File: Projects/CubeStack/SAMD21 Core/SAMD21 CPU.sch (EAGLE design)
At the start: 38 parts, among them Q1 MBT3904DW2T1, Q2 SI2347DS, Q3 SI2347DS, U1 ATSAMD21G-A, U2 SST26VF064B, U3 AZ1117C, X1A PINHD-1X10, X1B PINHD-1X10, X1C PINHD-1X10, X1D PINHD-1X10, X2 10PIN_CORTEX_DEBUGTHRU_HOLE, Y1 FC1610AN

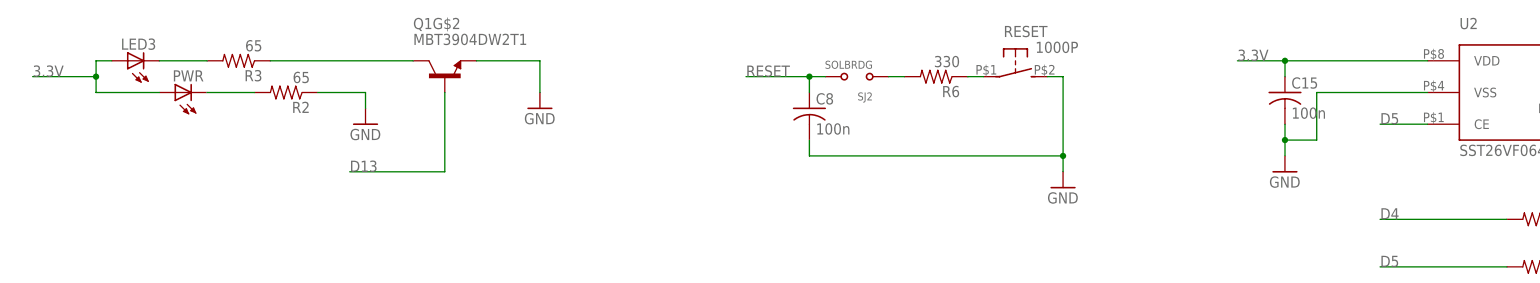
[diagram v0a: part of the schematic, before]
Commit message: Changed C9 package
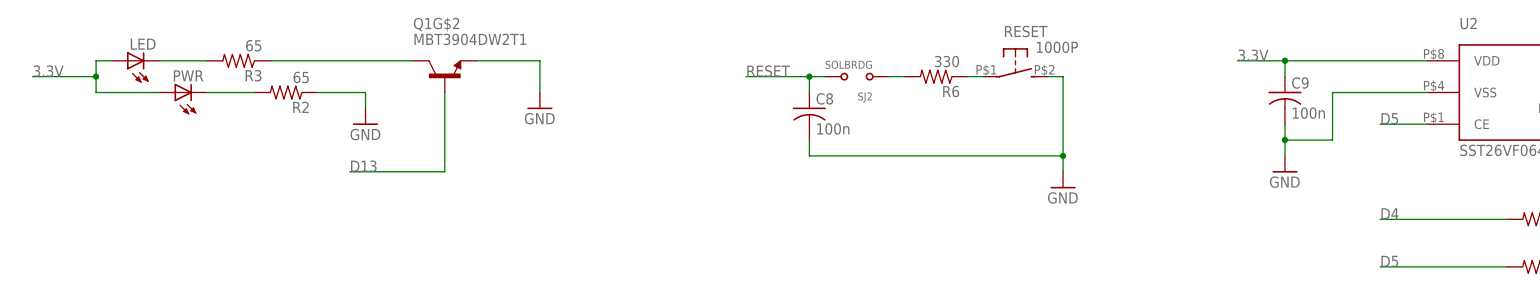
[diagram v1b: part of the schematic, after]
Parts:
- removed C15: 100n, resistor:C-USC0402
- added C9: 100n, resistor:C-USC0603
- renumbered LED3 to LED
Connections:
- net 3.3V: now also C9.1; no longer C15.1
- net GND: now also C9.2; no longer C15.2
